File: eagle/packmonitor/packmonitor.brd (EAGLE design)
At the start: 61.8 x 18 mm, 29 parts, among them IC1 24C64, IC2 TCA4311A, IC3 AVRXDA32TQFP, IC4 ACS712

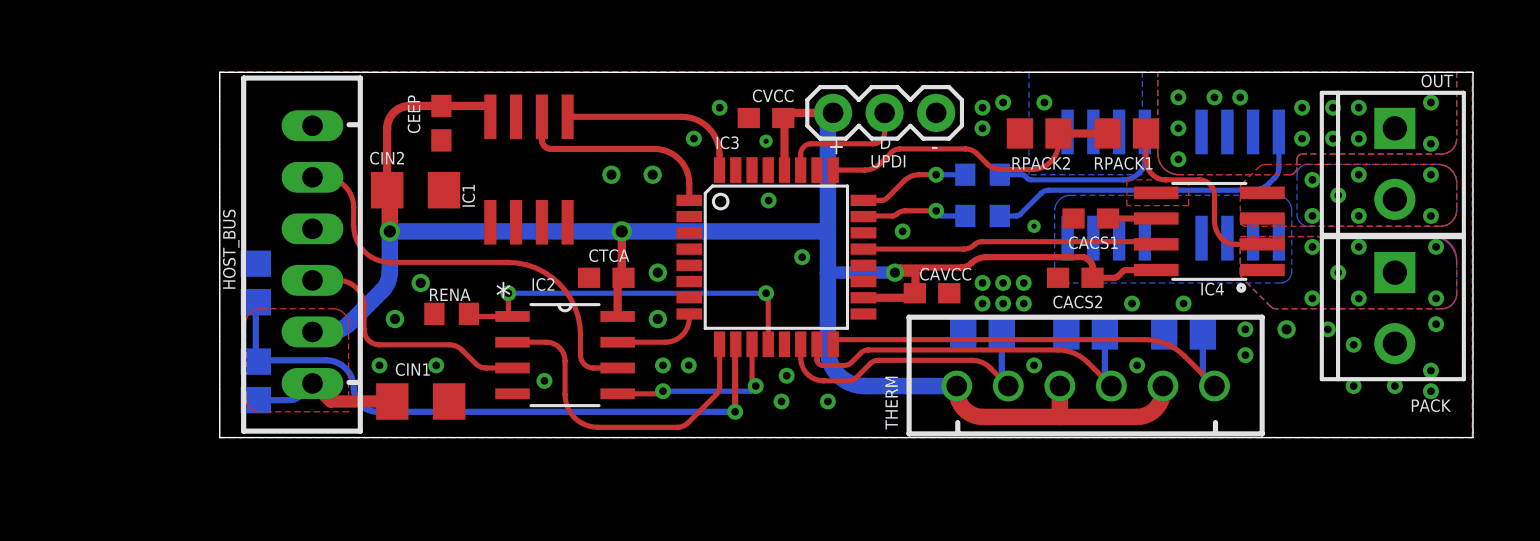
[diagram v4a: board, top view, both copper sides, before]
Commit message: Added pull up resistors on i2c busses
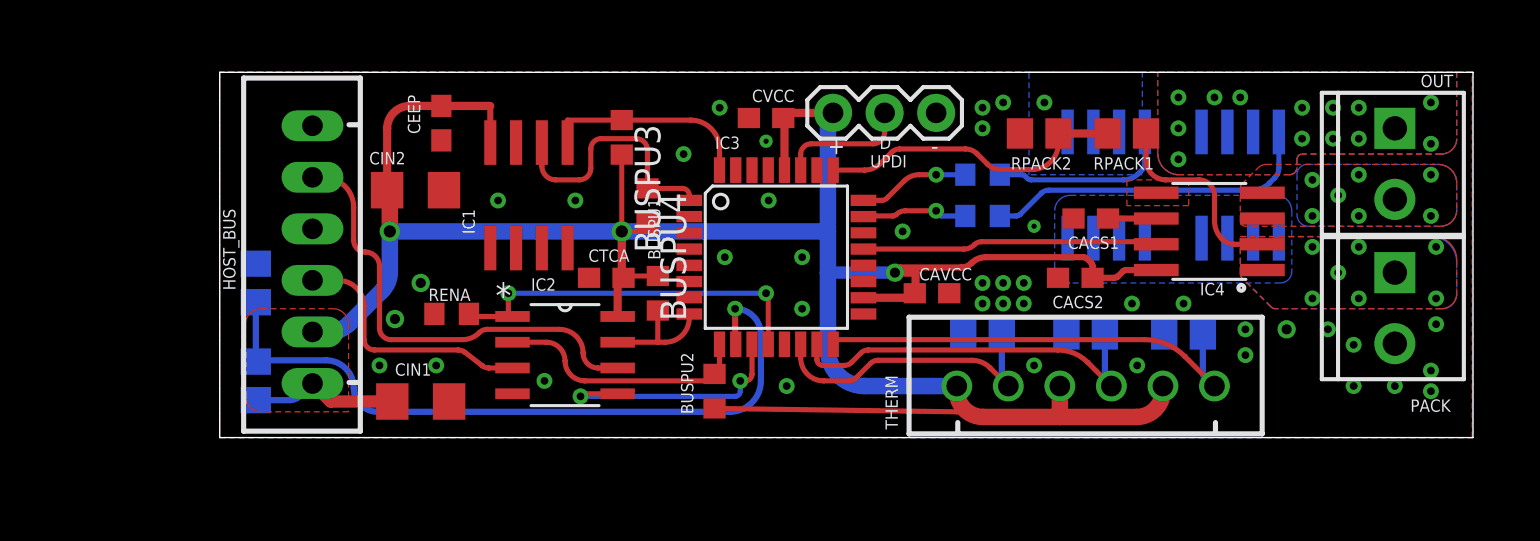
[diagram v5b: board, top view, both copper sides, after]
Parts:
- added BUSPU1, BUSPU2, BUSPU3, BUSPU4: 4K7, rcl:R0603
- moved IC1 1.27 mm to (15.7, 11.9)
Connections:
- net SCL_C: now also BUSPU2.1
- net SCL_H: now also BUSPU4.1
- net SDA_C: now also BUSPU1.1
- net SDA_H: now also BUSPU3.1
- net VCC: now also BUSPU1.2, BUSPU2.2, BUSPU3.2, BUSPU4.2
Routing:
- net VCC: track 111.1 -> 132.9 mm
- net VBUS: track 31.0 -> 35.4 mm
- net BUSREADY: track 9.10 -> 12.6 mm
- net SCL_C: track 15.9 -> 12.6 mm
- net SCL_H: track 10.1 -> 12.6 mm
- net SDAIN: track 20.0 -> 22.0 mm
- net SDA_C: track 4.23 -> 5.79 mm
- net SDA_H: track 9.03 -> 10.2 mm

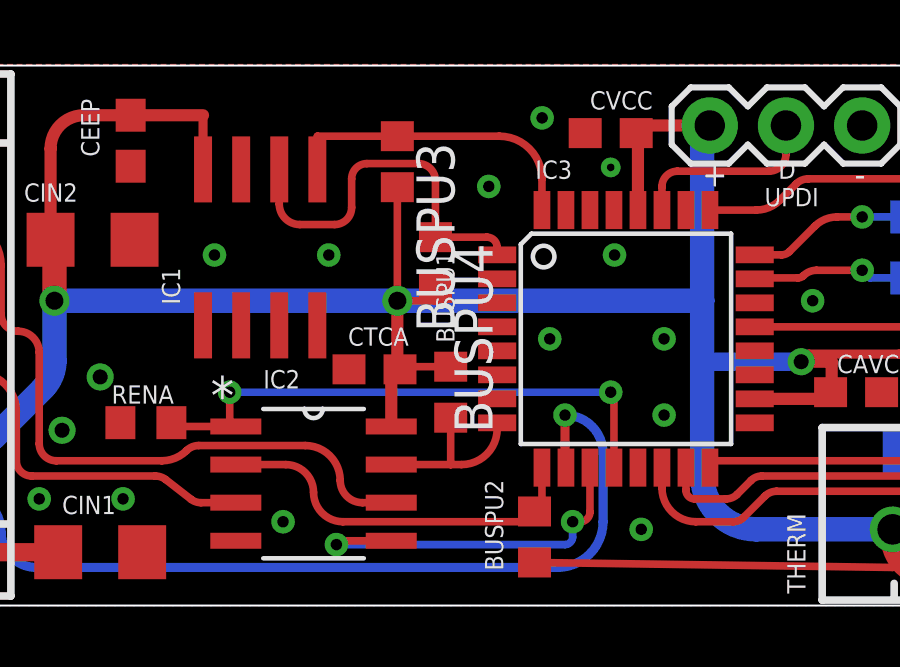
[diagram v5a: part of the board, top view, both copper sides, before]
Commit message: Cleanup labels for new resistors
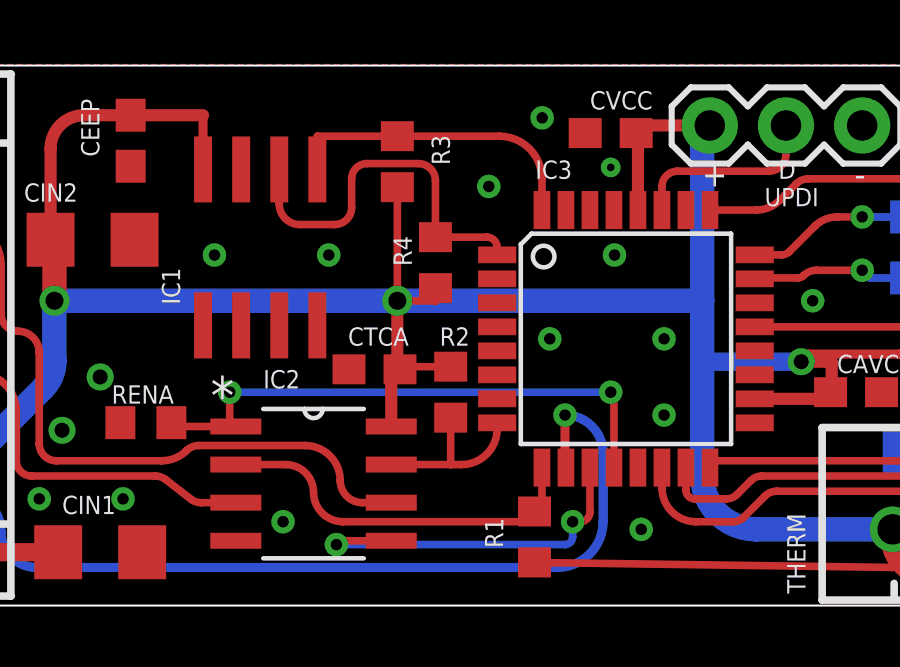
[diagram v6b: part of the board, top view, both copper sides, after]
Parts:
- renumbered BUSPU1 to R2, BUSPU2 to R1, BUSPU3 to R3, BUSPU4 to R4
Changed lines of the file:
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@@
 <grid distance="0.05" unitdist="inch" unit="inch" style="lines" multiple="1" display="no" altdistance="0.01" altunitdist="inch" altunit="inch"/>
 <layers>
-<layer number="1" name="Top" color="4" fill="1" visible="yes" active="yes"/>
+<layer number="1" name="Top" color="4" fill="1" visible="no" active="yes"/>
 <layer number="16" name="Bottom" color="1" fill="1" visible="yes" active="yes"/>
 <layer number="17" name="Pads" color="2" fill="1" visible="yes" active="yes"/>
@@
 <layer number="19" name="Unrouted" color="14" fill="1" visible="yes" active="yes"/>
 <layer number="20" name="Dimension" color="15" fill="1" visible="yes" active="yes"/>
-<layer number="21" name="tPlace" color="7" fill="1" visible="yes" active="yes"/>
+<layer number="21" name="tPlace" color="7" fill="1" visible="no" active="yes"/>
 <layer number="22" name="bPlace" color="7" fill="1" visible="yes" active="yes"/>
-<layer number="23" name="tOrigins" color="15" fill="1" visible="yes" active="yes"/>
+<layer number="23" name="tOrigins" color="15" fill="1" visible="no" active="yes"/>
 <layer number="24" name="bOrigins" color="15" fill="1" visible="yes" active="yes"/>
-<layer number="25" name="tNames" color="6" fill="1" visible="yes" active="yes"/>
+<layer number="25" name="tNames" color="6" fill="1" visible="no" active="yes"/>
 <layer number="26" name="bNames" color="5" fill="1" visible="yes" active="yes"/>
-<layer number="27" name="tValues" color="6" fill="1" visible="yes" active="yes"/>
+<layer number="27" name="tValues" color="6" fill="1" visible="no" active="yes"/>
 <layer number="28" name="bValues" color="5" fill="1" visible="yes" active="yes"/>
 <layer number="29" name="tStop" color="7" fill="3" visible="no" active="yes"/>
@@
 <attribute name="NAME" x="44.831" y="9.906" size="0.6096" layer="25" font="vector" ratio="12" rot="R180"/>
 </element>
-<element name="BUSPU1" library="rcl" package="R0603" value="4K7" x="22.098" y="7.112" smashed="yes" rot="R90">
-<attribute name="NAME" x="22.225" y="8.763" size="0.6096" layer="25" font="vector" ratio="14" rot="R90"/>
-</element>
-<element name="BUSPU2" library="rcl" package="R0603" value="4K7" x="24.892" y="2.286" smashed="yes" rot="R270">
-<attribute name="NAME" x="23.241" y="4.191" size="0.6096" layer="25" font="vector" ratio="14" rot="R270"/>
-</element>
-<element name="BUSPU3" library="rcl" package="R0603" value="4K7" x="20.32" y="14.7955" rot="R270"/>
-<element name="BUSPU4" library="rcl" package="R0603" value="4K7" x="21.59" y="11.43" rot="R270"/>
+<element name="R2" library="rcl" package="R0603" value="4K7" x="22.098" y="7.112" smashed="yes" rot="R90">
+<attribute name="NAME" x="22.733" y="9.271" size="0.6096" layer="25" font="vector" ratio="14" rot="R180"/>
+</element>
+<element name="R1" library="rcl" package="R0603" value="4K7" x="24.892" y="2.286" smashed="yes" rot="R270">
+<attribute name="NAME" x="23.241" y="2.921" size="0.6096" layer="25" font="vector" ratio="14" rot="R270"/>
+</element>
+<element name="R3" library="rcl" package="R0603" value="4K7" x="20.32" y="14.7955" smashed="yes" rot="R270">
+<attribute name="NAME" x="21.463" y="15.6845" size="0.6096" layer="25" font="vector" ratio="14" rot="R270"/>
+</element>
+<element name="R4" library="rcl" package="R0603" value="4K7" x="21.59" y="11.43" smashed="yes" rot="R270">
+<attribute name="NAME" x="20.193" y="12.319" size="0.6096" layer="25" font="vector" ratio="14" rot="R270"/>
+</element>
 </elements>
 <signals>
@@
 <vertex x="6.858" y="5.588"/>
 </polygon>
-<contactref element="BUSPU2" pad="2"/>
-<contactref element="BUSPU1" pad="2"/>
+<contactref element="R1" pad="2"/>
+<contactref element="R2" pad="2"/>
 <wire x1="24.892" y1="1.436" x2="36.83" y2="1.27" width="0.254" layer="1"/>
 <wire x1="36.83" y1="1.27" x2="36.83" y2="2.54" width="0.254" layer="1"/>
 <wire x1="22.098" y1="7.962" x2="20.408" y2="7.962" width="0.254" layer="1"/>
 <wire x1="20.408" y1="7.962" x2="20.408" y2="7.874" width="0.254" layer="1"/>
-<contactref element="BUSPU3" pad="2"/>
-<contactref element="BUSPU4" pad="2"/>
+<contactref element="R3" pad="2"/>
+<contactref element="R4" pad="2"/>
 <wire x1="20.32" y1="13.9455" x2="20.32" y2="10.16" width="0.254" layer="1"/>
 <wire x1="21.59" y1="10.58" x2="21.59" y2="10.16" width="0.3048" layer="1"/>
@@
 <contactref element="IC3" pad="32"/>
 <contactref element="IC1" pad="5"/>
-<contactref element="BUSPU3" pad="1"/>
+<contactref element="R3" pad="1"/>
 <wire x1="20.32" y1="15.6455" x2="17.653" y2="15.6455" width="0.254" layer="1"/>
 <wire x1="17.653" y1="15.6455" x2="17.653" y2="14.538" width="0.254" layer="1"/>
@@
 <contactref element="IC3" pad="1"/>
 <contactref element="IC1" pad="6"/>
-<contactref element="BUSPU4" pad="1"/>
+<contactref element="R4" pad="1"/>
 <wire x1="23.6474" y1="11.69" x2="23.6474" y2="11.937059375" width="0.254" layer="1"/>
 <wire x1="23.6474" y1="11.937059375" x2="23.304459375" y2="12.28" width="0.254" layer="1" curve="90"/>
@@
 <wire x1="22.45983125" y1="4.699" x2="23.6474" y2="5.88656875" width="0.254" layer="1" curve="90"/>
 <wire x1="23.6474" y1="5.88656875" x2="23.6474" y2="6.09" width="0.254" layer="1"/>
-<contactref element="BUSPU1" pad="1"/>
+<contactref element="R2" pad="1"/>
 <wire x1="22.098" y1="6.262" x2="22.098" y2="4.699" width="0.254" layer="1"/>
 </signal>
@@
 <wire x1="14.9352" y1="4.699" x2="16.601428125" y2="4.699" width="0.254" layer="1"/>
 <wire x1="16.601428125" y1="4.699" x2="17.526" y2="3.774428125" width="0.254" layer="1" curve="-90"/>
-<contactref element="BUSPU2" pad="1"/>
+<contactref element="R1" pad="1"/>
 <wire x1="24.638" y1="2.794" x2="24.892" y2="3.136" width="0.254" layer="1"/>
 <wire x1="24.892" y1="3.136" x2="25.14" y2="3.136" width="0.254" layer="1"/>

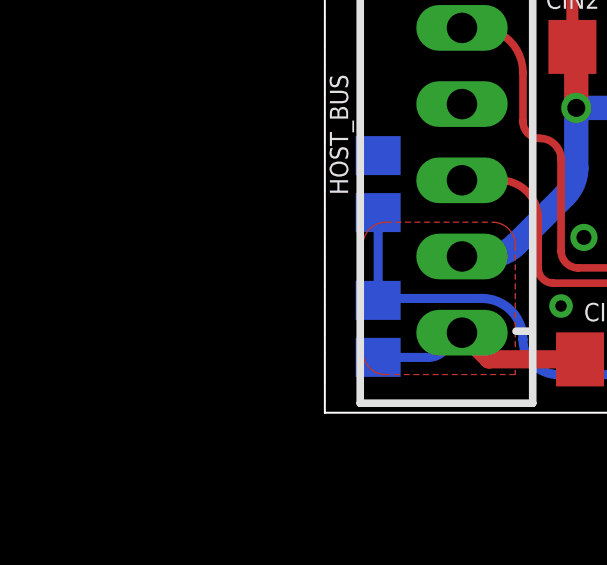
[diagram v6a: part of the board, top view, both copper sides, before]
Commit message: Added prevision 2.5v reference, need to get the shoehorn.
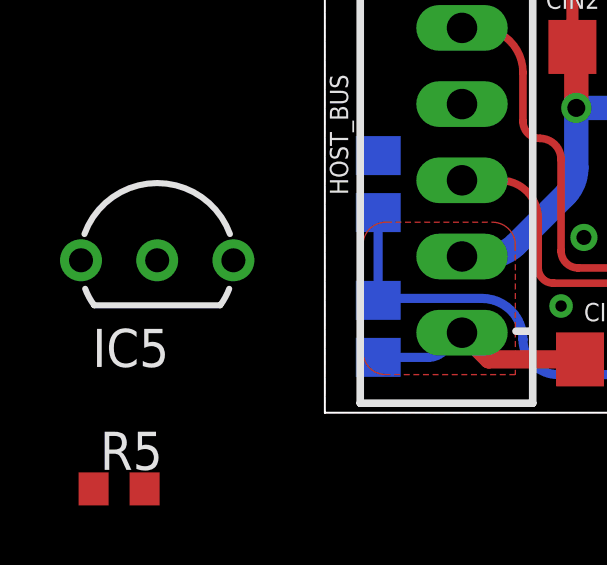
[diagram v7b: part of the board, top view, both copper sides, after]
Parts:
- added IC5: LM4041A12LP, texas:LP_O-PBCY-W3
- added R5: 4K7, rcl:R0603
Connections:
- new net N$4: IC3.17, IC5.2, R5.1
- net GND: now also IC5.3
- net VCC: now also R5.2
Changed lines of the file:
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@@
 <grid distance="0.05" unitdist="inch" unit="inch" style="lines" multiple="1" display="no" altdistance="0.01" altunitdist="inch" altunit="inch"/>
 <layers>
-<layer number="1" name="Top" color="4" fill="1" visible="no" active="yes"/>
+<layer number="1" name="Top" color="4" fill="1" visible="yes" active="yes"/>
 <layer number="16" name="Bottom" color="1" fill="1" visible="yes" active="yes"/>
 <layer number="17" name="Pads" color="2" fill="1" visible="yes" active="yes"/>
@@
 <layer number="19" name="Unrouted" color="14" fill="1" visible="yes" active="yes"/>
 <layer number="20" name="Dimension" color="15" fill="1" visible="yes" active="yes"/>
-<layer number="21" name="tPlace" color="7" fill="1" visible="no" active="yes"/>
+<layer number="21" name="tPlace" color="7" fill="1" visible="yes" active="yes"/>
 <layer number="22" name="bPlace" color="7" fill="1" visible="yes" active="yes"/>
-<layer number="23" name="tOrigins" color="15" fill="1" visible="no" active="yes"/>
+<layer number="23" name="tOrigins" color="15" fill="1" visible="yes" active="yes"/>
 <layer number="24" name="bOrigins" color="15" fill="1" visible="yes" active="yes"/>
-<layer number="25" name="tNames" color="6" fill="1" visible="no" active="yes"/>
+<layer number="25" name="tNames" color="6" fill="1" visible="yes" active="yes"/>
 <layer number="26" name="bNames" color="5" fill="1" visible="yes" active="yes"/>
-<layer number="27" name="tValues" color="6" fill="1" visible="no" active="yes"/>
+<layer number="27" name="tValues" color="6" fill="1" visible="yes" active="yes"/>
 <layer number="28" name="bValues" color="5" fill="1" visible="yes" active="yes"/>
 <layer number="29" name="tStop" color="7" fill="3" visible="no" active="yes"/>
@@
 <attribute name="NAME" x="20.193" y="12.319" size="0.6096" layer="25" font="vector" ratio="14" rot="R270"/>
 </element>
+<element name="IC5" library="texas" package="LP_O-PBCY-W3" value="LM4041A12LP" x="-5.08" y="5.08">
+<attribute name="OC_FARNELL" value="9486119" x="-5.08" y="5.08" size="0.6096" layer="27" font="vector" ratio="14" display="off"/>
+<attribute name="MPN" value="" x="-5.08" y="5.08" size="0.6096" layer="27" font="vector" ratio="14" display="off"/>
+<attribute name="MF" value="" x="-5.08" y="5.08" size="0.6096" layer="27" font="vector" ratio="14" display="off"/>
+<attribute name="OC_NEWARK" value="unknown" x="-5.08" y="5.08" size="0.6096" layer="27" font="vector" ratio="14" display="off"/>
+</element>
+<element name="R5" library="rcl" package="R0603" value="4K7" x="-6.35" y="-2.54"/>
 </elements>
 <signals>
@@
 <wire x1="21.59" y1="10.58" x2="21.59" y2="10.16" width="0.3048" layer="1"/>
 <wire x1="21.59" y1="10.16" x2="20.32" y2="10.16" width="0.254" layer="1"/>
+<contactref element="R5" pad="2"/>
+<wire x1="2.286" y1="1.844" x2="-5.5" y2="-2.54" width="0" layer="19" extent="1-16"/>
 </signal>
 <signal name="GND">
@@
 <via x="25.4" y="8.89" extent="1-16" drill="0.381"/>
 <via x="29.21" y="6.35" extent="1-16" drill="0.381"/>
+<contactref element="IC5" pad="3"/>
+<wire x1="2.286" y1="8.57" x2="-2.54" y2="5.08" width="0" layer="19" extent="16-16"/>
 </signal>
 <signal name="UPDI">
@@
 <wire x1="44.284" y1="10.795" x2="46.6598" y2="10.795" width="0.3048" layer="1"/>
 </signal>
+<signal name="N$4">
+<contactref element="IC3" pad="17"/>
+<contactref element="IC5" pad="2"/>
+<contactref element="R5" pad="1"/>
+<wire x1="-5.08" y1="5.08" x2="32.2326" y2="6.09" width="0" layer="19" extent="1-1"/>
+<wire x1="-7.2" y1="-2.54" x2="-5.08" y2="5.08" width="0" layer="19" extent="1-1"/>
+</signal>
 </signals>
